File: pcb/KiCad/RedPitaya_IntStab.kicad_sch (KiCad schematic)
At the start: 28 parts, among them J1 C64AC, J16 Hold_2, J4 Hold_1

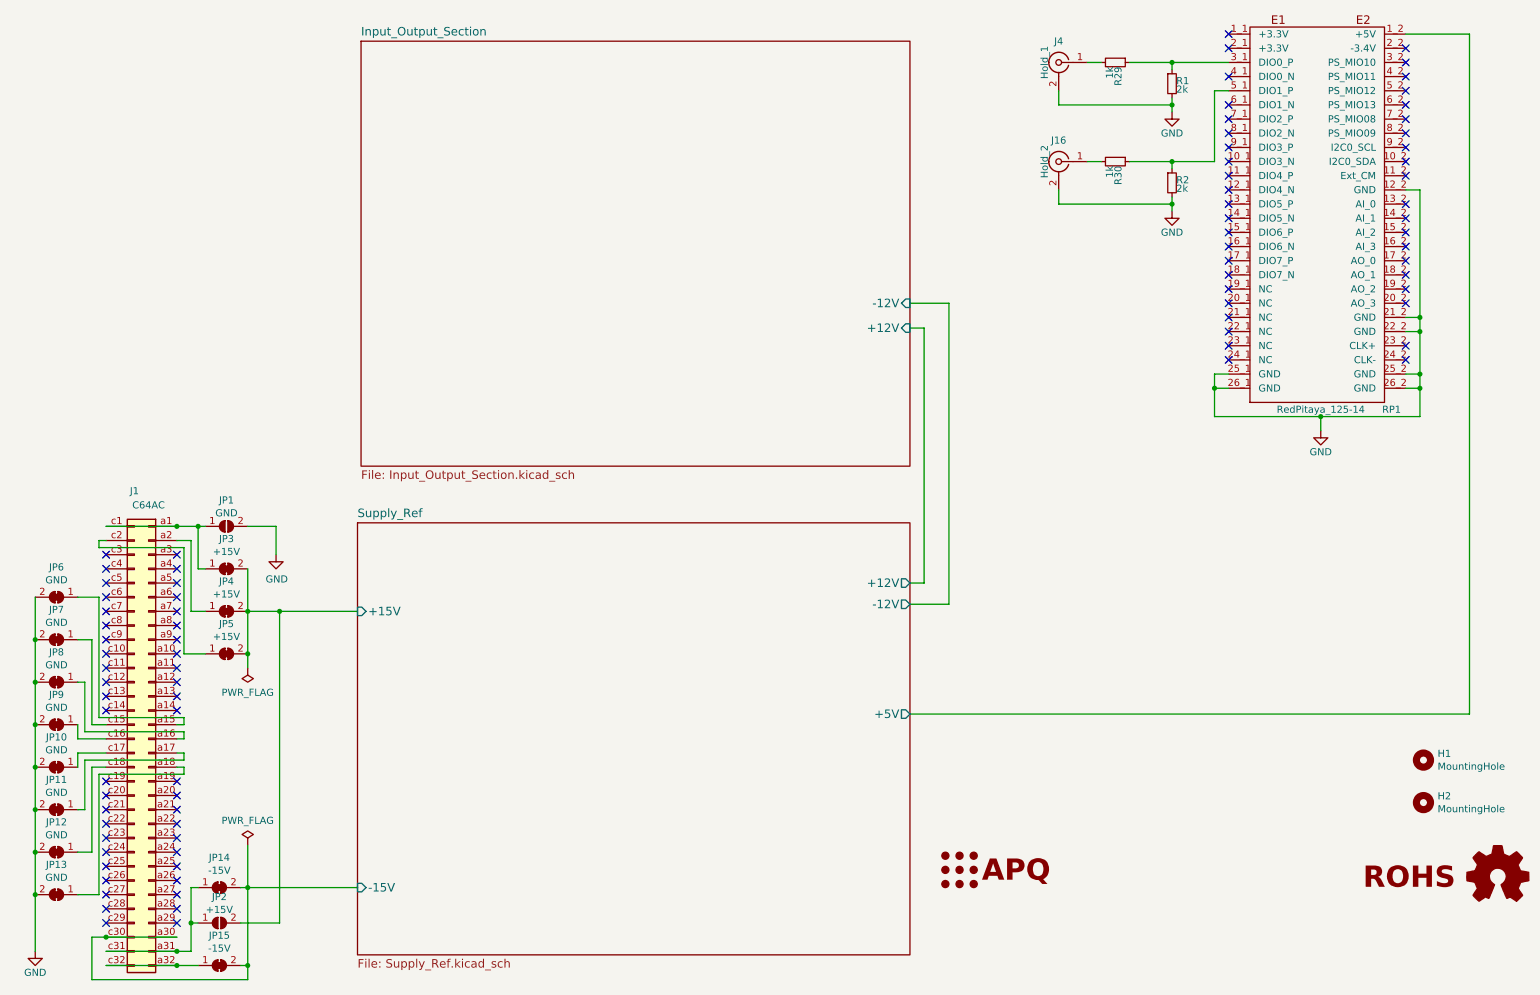
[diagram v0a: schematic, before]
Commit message: Fixed off-grid positioning
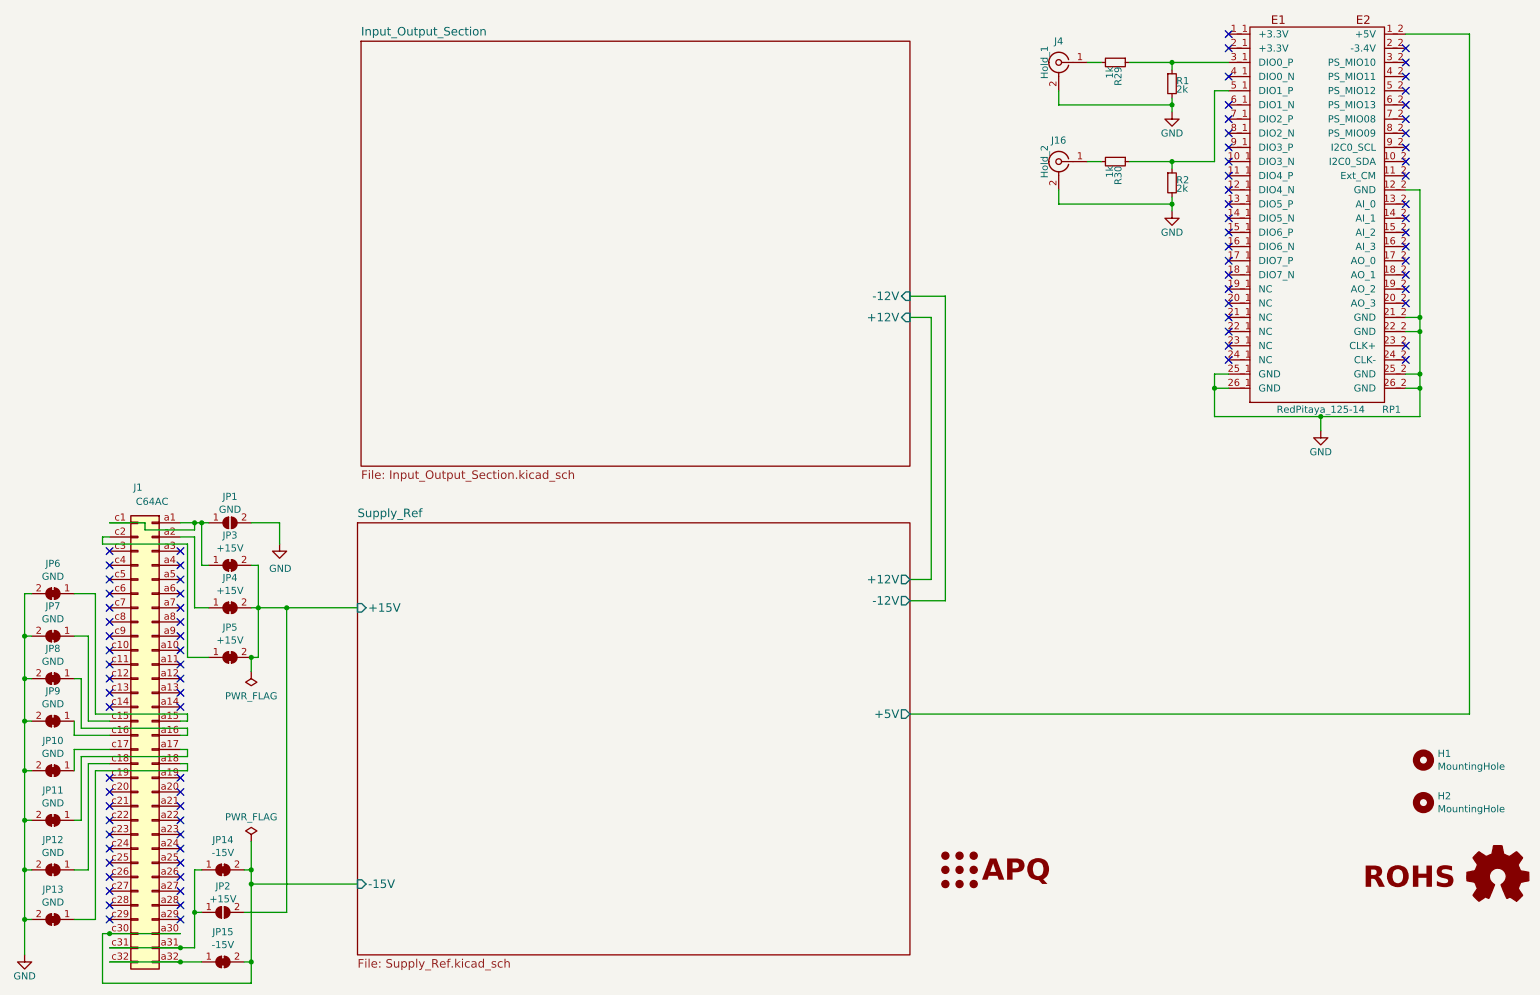
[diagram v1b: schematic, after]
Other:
- moved on the sheet: J1, JP1, JP10, JP11, JP12, JP13, JP14, JP15, JP2, JP3, JP4, JP5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
